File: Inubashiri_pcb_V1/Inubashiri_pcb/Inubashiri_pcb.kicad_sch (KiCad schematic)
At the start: 5 parts, among them U1 ESP32-DEVKITC-32E, U2 E220-900T22S_JP_CLEALINK_MODU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, U3 NEO-6M_GPS_MODULE, U4 NEO-6M_GPS_MODULE, U6 NEO-6M_GPS_MODULE

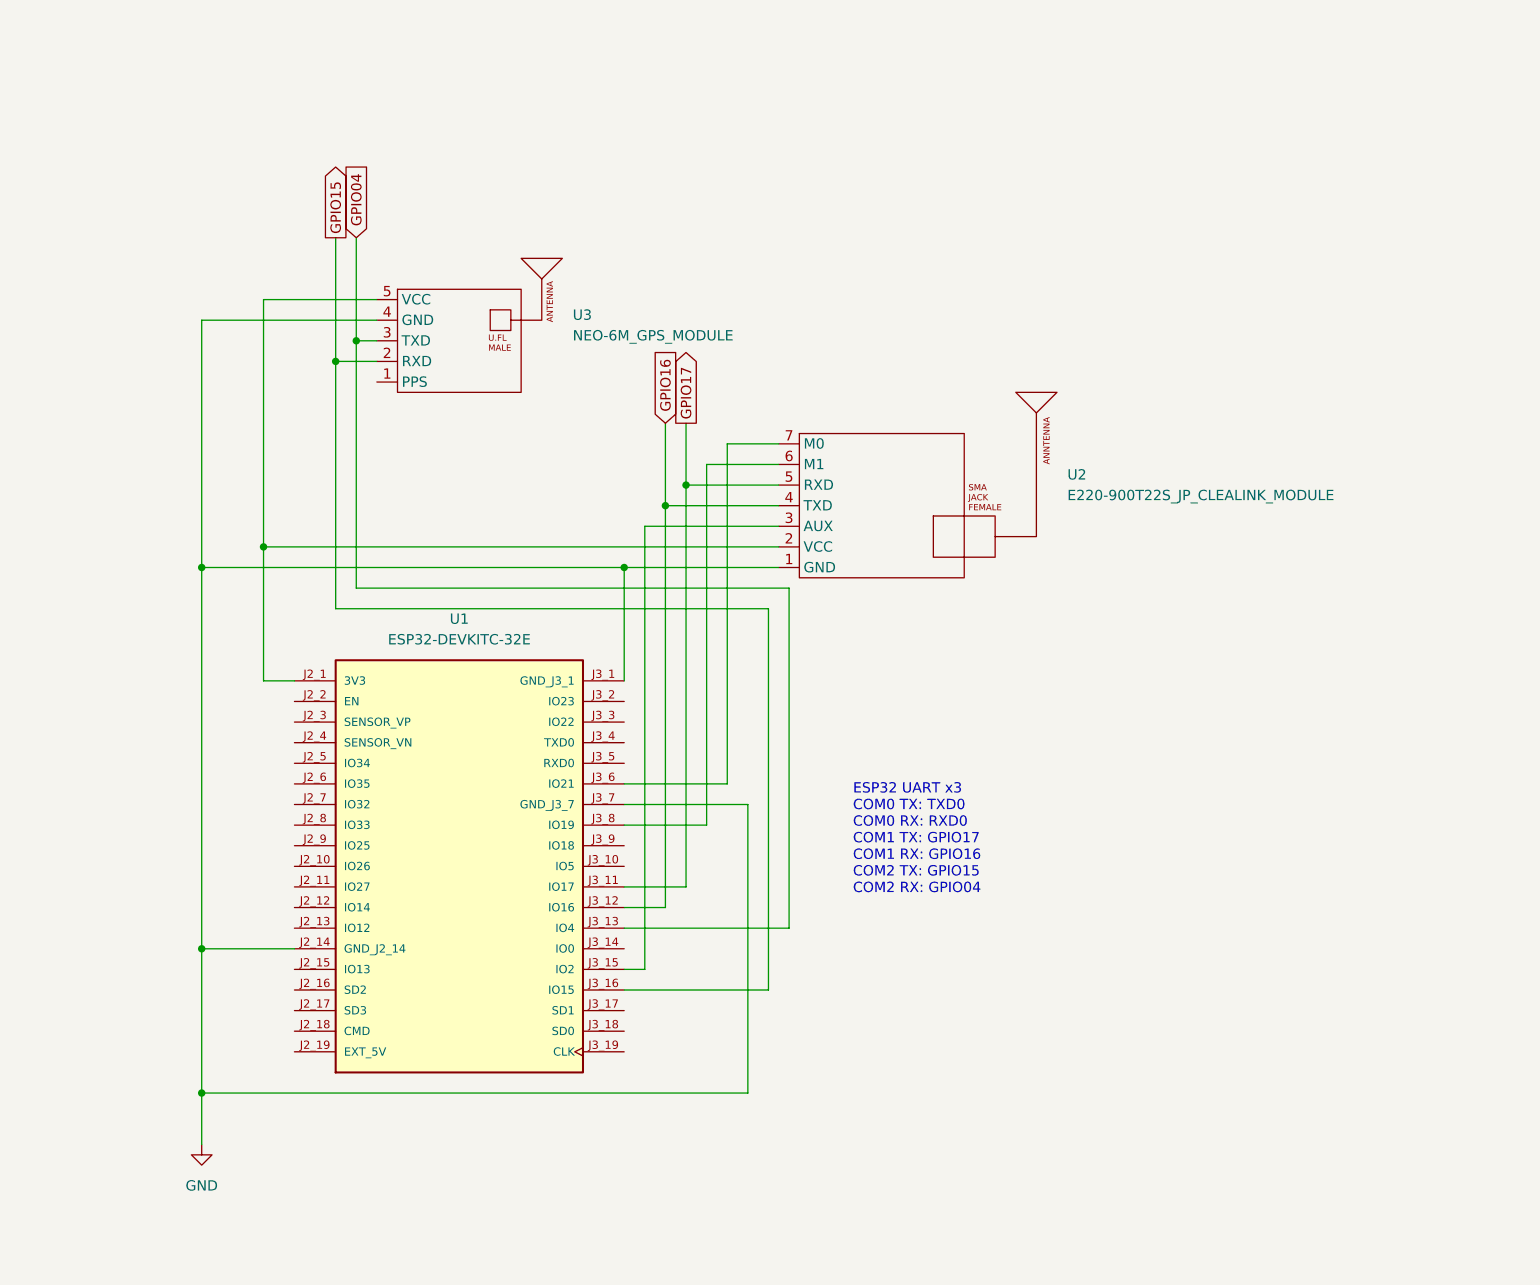
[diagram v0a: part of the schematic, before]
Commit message: add schematic pdf
add schematic pdf
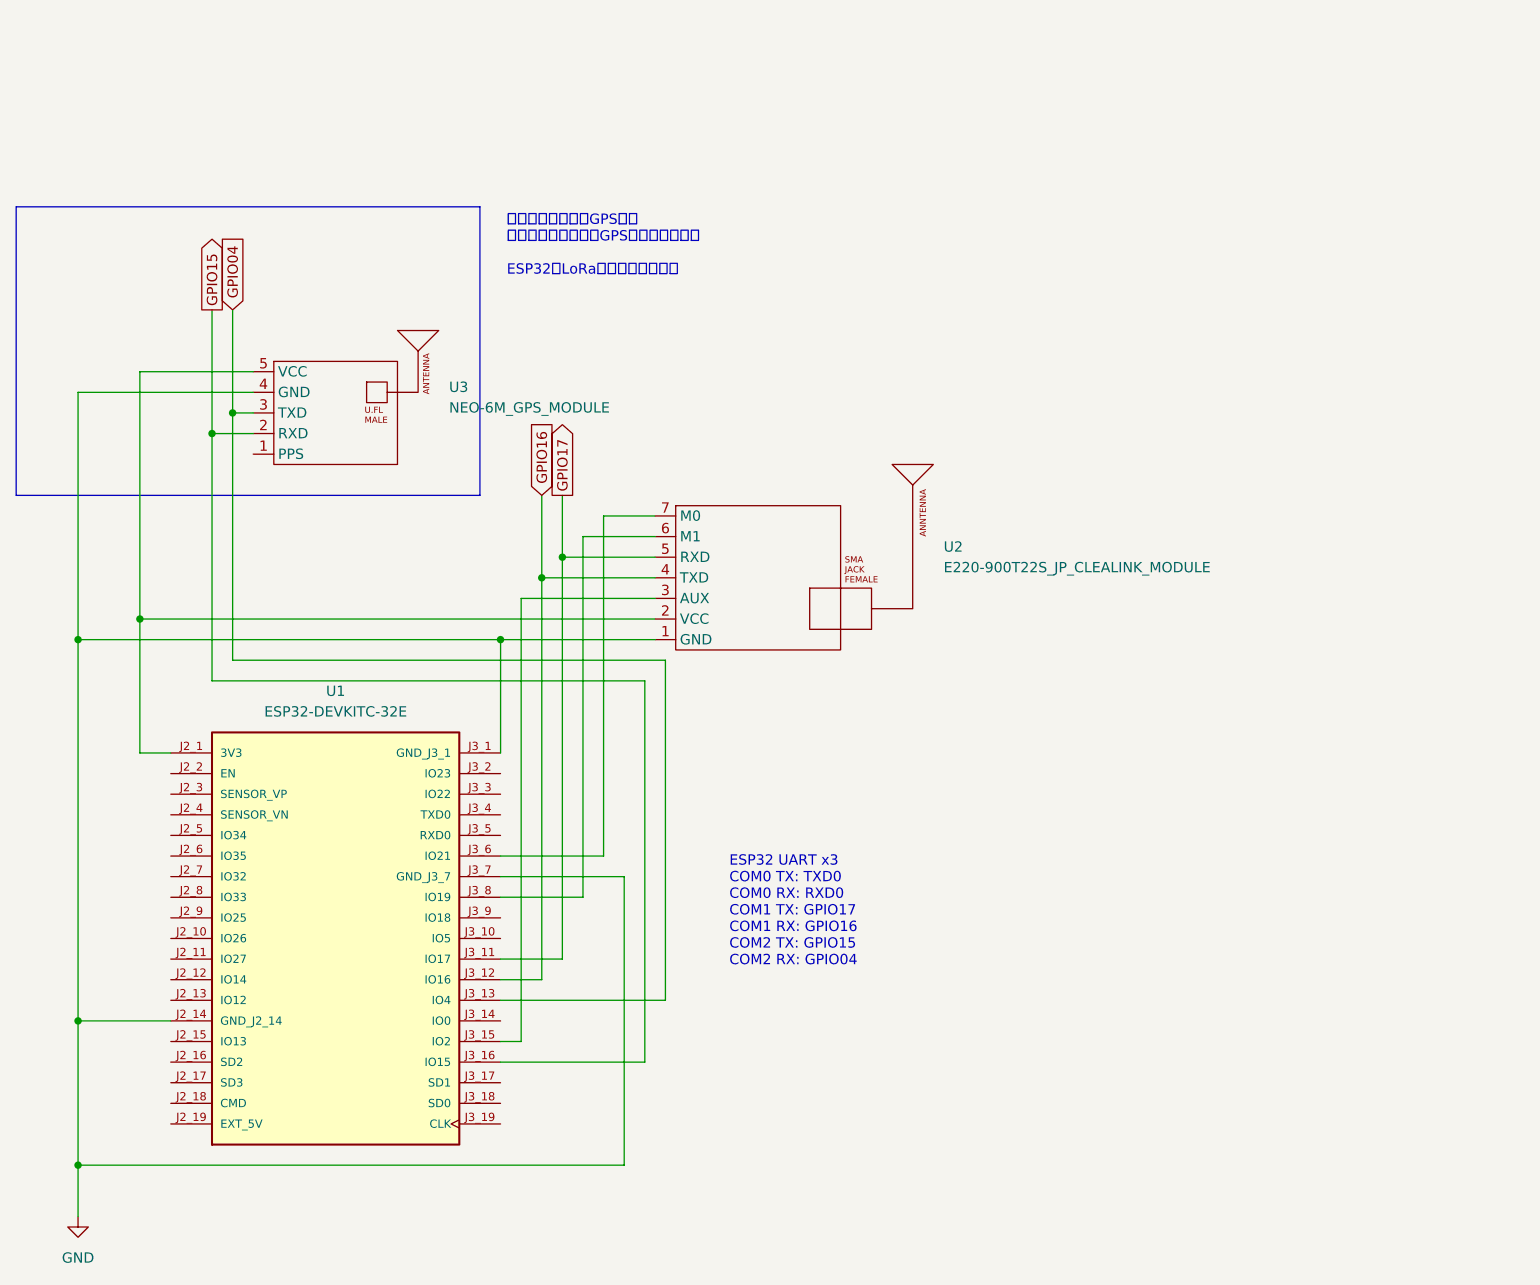
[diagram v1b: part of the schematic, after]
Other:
- note added: "送信側（犬側）：GPSあり 受信側（人間側）：GPSモジュールなし ESP32とLoRaモジュールは共通"
- company: (none) -> takurx
- title: (none) -> Inubashiri PCB
- moved on the sheet: U1, U2, U3

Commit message: add v1.1 schematic
add v1.1 schematic
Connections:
- net GPIO14: now reaches U1.J2_12 (IO14)
- net GPIO14: now also U3.2 (RXD)
- net GPIO12: now reaches U1.J2_13 (IO12)
- net GPIO12: now also U3.3 (TXD)
- net GPIO04: no longer names the net of U1.J3_13 (IO4)
- net GPIO04: no longer U3.3 (TXD)
- net GPIO15: no longer names the net of U1.J3_16 (IO15)
- net GPIO15: no longer U3.2 (RXD)
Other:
- note added: "ESP32 UART x3 COM0 RX: RXD0, GPIO3 COM0 TX: TXD0, GPIO1 COM1 RX: GPIO9 -> GPIO12 COM1 TX: GPIO10 -> GPIO14 COM2 RX: GPIO16 COM2 TX: GPIO17"
- note removed: "ESP32 UART x3 COM0 TX: TXD0 COM0 RX: RXD0 COM1 TX: GPIO17 COM1 RX: GPIO16 COM2 TX: GPIO15 COM2 RX: GPIO04"
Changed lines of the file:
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@@
 	(title_block
 		(title "Inubashiri PCB")
-		(date "2025-10-22")
-		(rev "V1")
+		(date "2025-11-03")
+		(rev "V1.1")
 		(company "takurx")
 	)
@@
 		)
 	)
-	(text "ESP32 UART x3\nCOM0 TX: TXD0\nCOM0 RX: RXD0\nCOM1 TX: GPIO17\nCOM1 RX: GPIO16\nCOM2 TX: GPIO15\nCOM2 RX: GPIO04"
+	(text "ESP32 UART x3\nCOM0 RX: RXD0, GPIO3\nCOM0 TX: TXD0, GPIO1\n\nCOM1 RX: GPIO9  -> GPIO12\nCOM1 TX: GPIO10 -> GPIO14\n\nCOM2 RX: GPIO16\nCOM2 TX: GPIO17"
 		(exclude_from_sim no)
 		(at 179.324 118.618 0)
@@
 	)
 	(junction
+		(at 158.75 74.93)
+		(diameter 0)
+		(color 0 0 0 0)
+	)
+	(junction
+		(at 99.06 85.09)
+		(diameter 0)
+		(color 0 0 0 0)
+	)
+	(junction
+		(at 106.68 82.55)
+		(diameter 0)
+		(color 0 0 0 0)
+	)
+	(junction
+		(at 99.06 149.86)
+		(diameter 0)
+		(color 0 0 0 0)
+	)
+	(junction
+		(at 156.21 77.47)
+		(diameter 0)
+		(color 0 0 0 0)
+	)
+	(junction
 		(at 118.11 57.15)
 		(diameter 0)
@@
 	)
 	(junction
-		(at 158.75 74.93)
+		(at 99.06 132.08)
+		(diameter 0)
+		(color 0 0 0 0)
+	)
+	(junction
+		(at 151.13 85.09)
 		(diameter 0)
 		(color 0 0 0 0)
@@
 		(color 0 0 0 0)
 	)
-	(junction
-		(at 99.06 85.09)
-		(diameter 0)
-		(color 0 0 0 0)
-	)
-	(junction
-		(at 106.68 82.55)
-		(diameter 0)
-		(color 0 0 0 0)
-	)
-	(junction
-		(at 99.06 149.86)
-		(diameter 0)
-		(color 0 0 0 0)
-	)
-	(junction
-		(at 156.21 77.47)
-		(diameter 0)
-		(color 0 0 0 0)
-	)
-	(junction
-		(at 99.06 132.08)
-		(diameter 0)
-		(color 0 0 0 0)
-	)
-	(junction
-		(at 151.13 85.09)
-		(diameter 0)
-		(color 0 0 0 0)
-	)
 	(wire
 		(pts
@@
 	(wire
 		(pts
+			(xy 115.57 59.69) (xy 93.98 59.69)
+		)
+		(stroke
+			(width 0)
+			(type default)
+		)
+	)
+	(wire
+		(pts
 			(xy 99.06 54.61) (xy 99.06 85.09)
 		)
@@
 	(wire
 		(pts
-			(xy 171.45 129.54) (xy 151.13 129.54)
-		)
-		(stroke
-			(width 0)
-			(type default)
-		)
-	)
-	(wire
-		(pts
-			(xy 115.57 90.17) (xy 115.57 59.69)
-		)
-		(stroke
-			(width 0)
-			(type default)
-		)
-	)
-	(wire
-		(pts
 			(xy 151.13 85.09) (xy 151.13 99.06)
 		)
@@
 	(wire
 		(pts
+			(xy 93.98 127) (xy 110.49 127)
+		)
+		(stroke
+			(width 0)
+			(type default)
+		)
+	)
+	(wire
+		(pts
+			(xy 96.52 129.54) (xy 110.49 129.54)
+		)
+		(stroke
+			(width 0)
+			(type default)
+		)
+	)
+	(wire
+		(pts
 			(xy 106.68 82.55) (xy 106.68 99.06)
 		)
@@
 	(wire
 		(pts
-			(xy 151.13 137.16) (xy 168.91 137.16)
+			(xy 96.52 57.15) (xy 96.52 129.54)
 		)
 		(stroke
@@
 	(wire
 		(pts
-			(xy 118.11 57.15) (xy 118.11 87.63)
-		)
-		(stroke
-			(width 0)
-			(type default)
-		)
-	)
-	(wire
-		(pts
 			(xy 115.57 59.69) (xy 120.65 59.69)
 		)
@@
 	(wire
 		(pts
-			(xy 168.91 90.17) (xy 115.57 90.17)
-		)
-		(stroke
-			(width 0)
-			(type default)
-		)
-	)
-	(wire
-		(pts
-			(xy 168.91 137.16) (xy 168.91 90.17)
-		)
-		(stroke
-			(width 0)
-			(type default)
-		)
-	)
-	(wire
-		(pts
 			(xy 170.18 74.93) (xy 158.75 74.93)
 		)
@@
 	(wire
 		(pts
+			(xy 118.11 57.15) (xy 96.52 57.15)
+		)
+		(stroke
+			(width 0)
+			(type default)
+		)
+	)
+	(wire
+		(pts
 			(xy 151.13 114.3) (xy 166.37 114.3)
 		)
@@
 	(wire
 		(pts
-			(xy 171.45 87.63) (xy 171.45 129.54)
-		)
-		(stroke
-			(width 0)
-			(type default)
-		)
-	)
-	(wire
-		(pts
 			(xy 158.75 67.31) (xy 158.75 74.93)
 		)
@@
 	(wire
 		(pts
-			(xy 118.11 87.63) (xy 171.45 87.63)
+			(xy 93.98 59.69) (xy 93.98 127)
 		)
 		(stroke
@@
 		)
 	)
-	(global_label "GPIO15"
+	(global_label "GPIO14"
 		(shape output)
 		(at 115.57 44.45 90)
@@
 		)
 	)
-	(global_label "GPIO04"
+	(global_label "GPIO12"
 		(shape input)
 		(at 118.11 44.45 90)

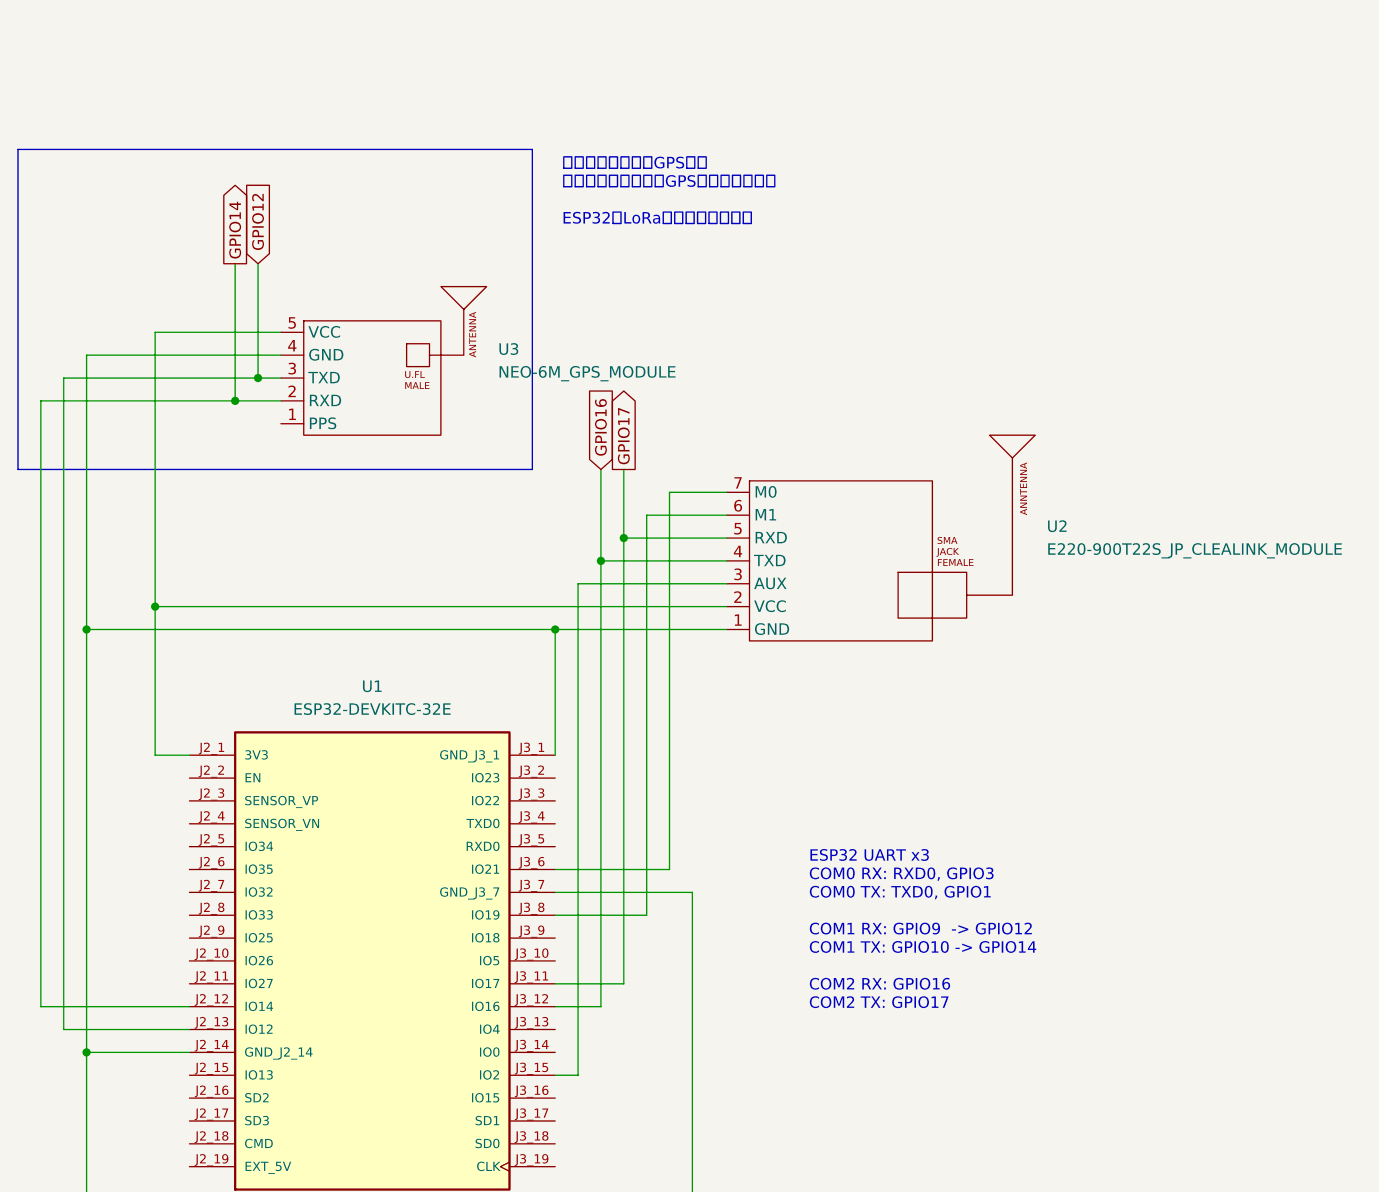
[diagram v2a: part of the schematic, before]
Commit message: fix #18, change pin assignment
fix #18, change pin assignment
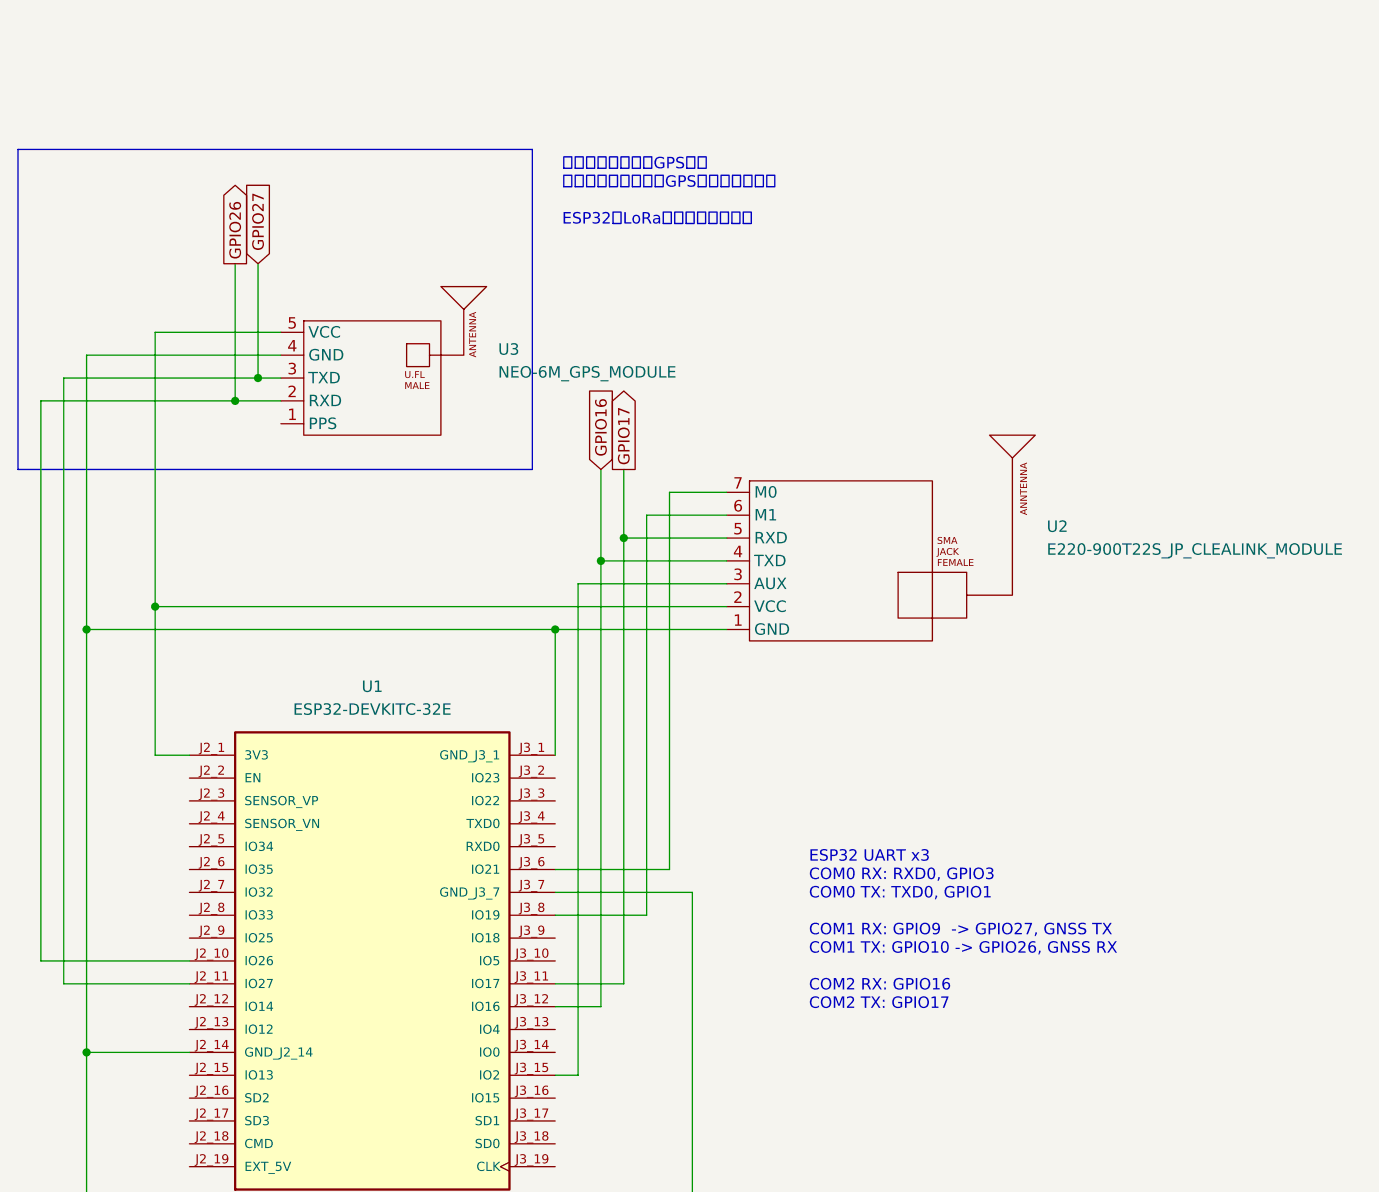
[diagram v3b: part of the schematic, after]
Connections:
- net GPIO26: now reaches U1.J2_10 (IO26)
- net GPIO26: now also U3.2 (RXD)
- net GPIO27: now reaches U1.J2_11 (IO27)
- net GPIO27: now also U3.3 (TXD)
- net GPIO12: no longer names the net of U1.J2_13 (IO12)
- net GPIO12: no longer U3.3 (TXD)
- net GPIO14: no longer names the net of U1.J2_12 (IO14)
- net GPIO14: no longer U3.2 (RXD)
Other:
- note added: "ESP32 UART x3 COM0 RX: RXD0, GPIO3 COM0 TX: TXD0, GPIO1 COM1 RX: GPIO9 -> GPIO27, GNSS TX COM1 TX: GPIO10 -> GPIO26, GNSS RX COM2 RX: GPIO16 COM2 TX: GPIO17"
- note removed: "ESP32 UART x3 COM0 RX: RXD0, GPIO3 COM0 TX: TXD0, GPIO1 COM1 RX: GPIO9 -> GPIO12 COM1 TX: GPIO10 -> GPIO14 COM2 RX: GPIO16 COM2 TX: GPIO17"
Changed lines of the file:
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@@
 		(title "Inubashiri PCB")
 		(date "2025-11-03")
-		(rev "V1.1")
+		(rev "V1.2")
 		(company "takurx")
 	)
@@
 		)
 	)
-	(text "ESP32 UART x3\nCOM0 RX: RXD0, GPIO3\nCOM0 TX: TXD0, GPIO1\n\nCOM1 RX: GPIO9  -> GPIO12\nCOM1 TX: GPIO10 -> GPIO14\n\nCOM2 RX: GPIO16\nCOM2 TX: GPIO17"
+	(text "ESP32 UART x3\nCOM0 RX: RXD0, GPIO3\nCOM0 TX: TXD0, GPIO1\n\nCOM1 RX: GPIO9  -> GPIO27, GNSS TX\nCOM1 TX: GPIO10 -> GPIO26, GNSS RX\n\nCOM2 RX: GPIO16\nCOM2 TX: GPIO17"
 		(exclude_from_sim no)
 		(at 179.324 118.618 0)
@@
 	(wire
 		(pts
-			(xy 93.98 127) (xy 110.49 127)
-		)
-		(stroke
-			(width 0)
-			(type default)
-		)
-	)
-	(wire
-		(pts
-			(xy 96.52 129.54) (xy 110.49 129.54)
-		)
-		(stroke
-			(width 0)
-			(type default)
-		)
-	)
-	(wire
-		(pts
 			(xy 106.68 82.55) (xy 106.68 99.06)
 		)
@@
 	(wire
 		(pts
-			(xy 96.52 57.15) (xy 96.52 129.54)
-		)
-		(stroke
-			(width 0)
-			(type default)
-		)
-	)
-	(wire
-		(pts
 			(xy 161.29 116.84) (xy 151.13 116.84)
 		)
@@
 	(wire
 		(pts
+			(xy 93.98 121.92) (xy 93.98 59.69)
+		)
+		(stroke
+			(width 0)
+			(type default)
+		)
+	)
+	(wire
+		(pts
 			(xy 170.18 74.93) (xy 158.75 74.93)
 		)
@@
 	(wire
 		(pts
+			(xy 110.49 121.92) (xy 93.98 121.92)
+		)
+		(stroke
+			(width 0)
+			(type default)
+		)
+	)
+	(wire
+		(pts
+			(xy 96.52 124.46) (xy 96.52 57.15)
+		)
+		(stroke
+			(width 0)
+			(type default)
+		)
+	)
+	(wire
+		(pts
 			(xy 118.11 57.15) (xy 96.52 57.15)
 		)
@@
 	(wire
 		(pts
+			(xy 110.49 124.46) (xy 96.52 124.46)
+		)
+		(stroke
+			(width 0)
+			(type default)
+		)
+	)
+	(wire
+		(pts
 			(xy 158.75 67.31) (xy 158.75 74.93)
-		)
-		(stroke
-			(width 0)
-			(type default)
-		)
-	)
-	(wire
-		(pts
-			(xy 93.98 59.69) (xy 93.98 127)
 		)
 		(stroke
@@
 		)
 	)
-	(global_label "GPIO14"
+	(global_label "GPIO26"
 		(shape output)
 		(at 115.57 44.45 90)
@@
 		)
 	)
-	(global_label "GPIO12"
+	(global_label "GPIO27"
 		(shape input)
 		(at 118.11 44.45 90)
